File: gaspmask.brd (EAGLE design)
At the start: 25.4 x 25.4 mm, 9 parts, among them IC1 PIC12F629P, U1 BMP180

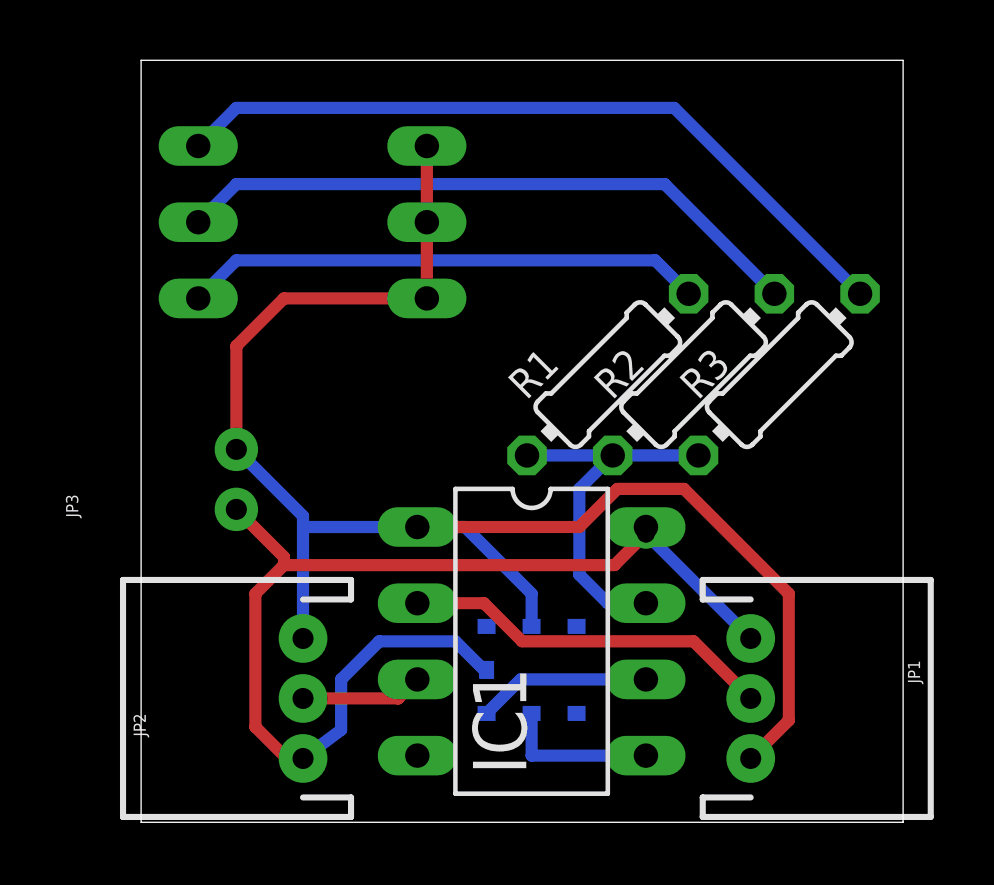
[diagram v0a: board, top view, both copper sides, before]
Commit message: Revised to take cheap chinese daughter board.
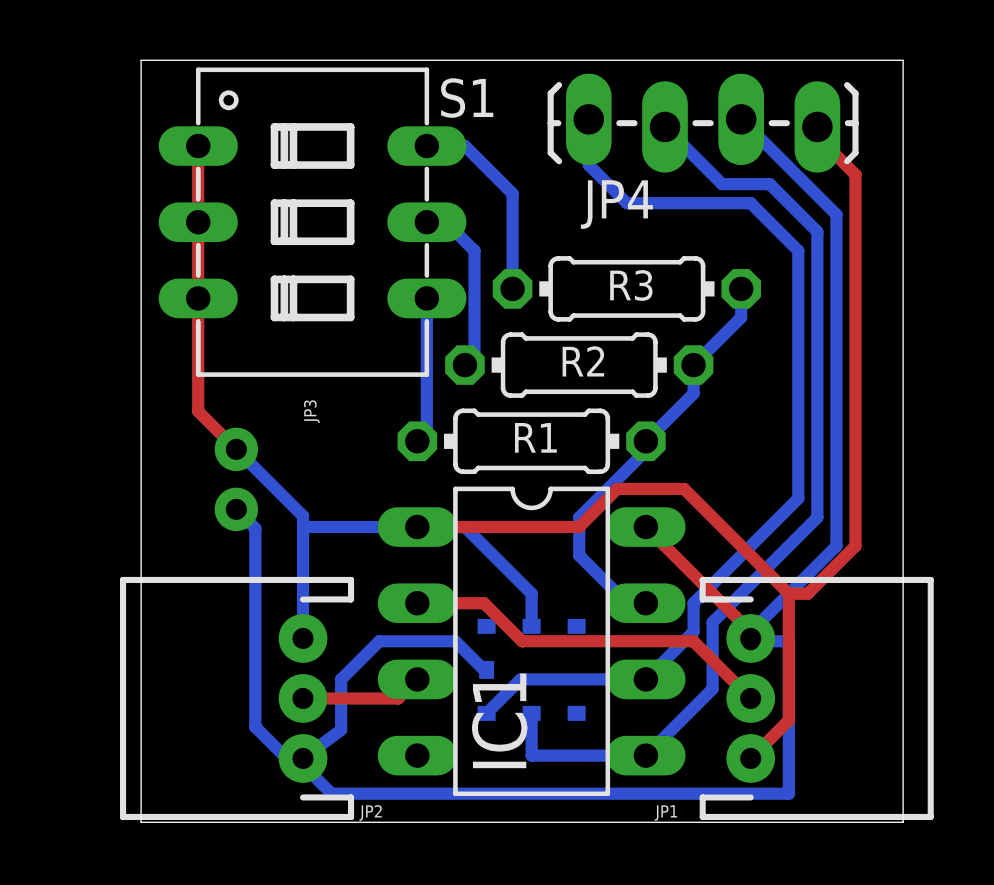
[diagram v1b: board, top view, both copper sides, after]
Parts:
- added JP4: (no value), SparkFun-Connectors:1X04_LOCK_LONGPADS
- moved R3 5.83 mm to (16.2, 17.8), turned to 180 degrees
- moved R2 3.82 mm to (14.6, 15.2), turned to 180 degrees
- moved R1 3.38 mm to (13.0, 12.7), turned to 180 degrees
- flipped S1 to the top
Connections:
- removed net N$4: IC1.5, U1.5
- removed net N$5: IC1.6, U1.6
- new net SCL: IC1.5, JP4.3, U1.5
- new net SDA: IC1.6, JP4.4, U1.6
- net +5V: now also JP4.1
- net GND: now also JP4.2
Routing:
- net SDA: track 0.00 -> 31.9 mm
- net SCL: track 0.00 -> 31.6 mm
- net GND: track 37.0 -> 66.8 mm
- net N$8: track 25.2 -> 6.69 mm
- net N$7: track 21.2 -> 5.92 mm
- net +5V: track 52.8 -> 65.2 mm
- net N$6: track 17.3 -> 4.89 mm
- net N$5: track 5.78 -> 0.00 mm
- net N$4: track 5.22 -> 0.00 mm
- net N$9: track 12.8 -> 14.0 mm
